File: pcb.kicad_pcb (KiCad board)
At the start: 2 copper layers, 65 x 56 mm, 37 parts, among them J1 Raspberry_Pi_2_3, J10 Conn_01x03_Male, J2 Conn_01x03_Male, J3 Conn_01x03_Male, J4 Conn_01x02_Male, J5 Conn_01x02_Male, J6 Conn_01x03_Male, J7 Conn_01x05_Male, J8 Conn_01x03_Male, J9 Conn_01x03_Male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

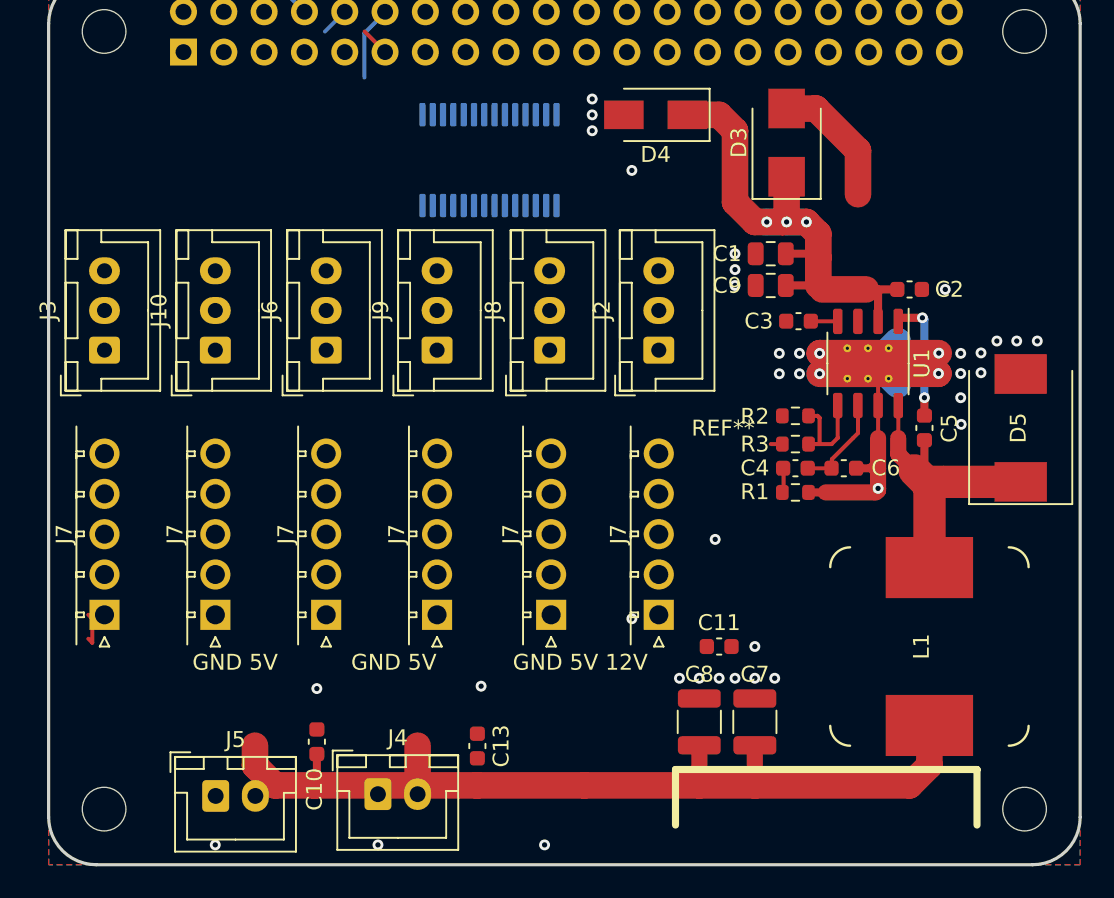
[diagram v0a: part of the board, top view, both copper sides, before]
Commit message: added images & plug placement
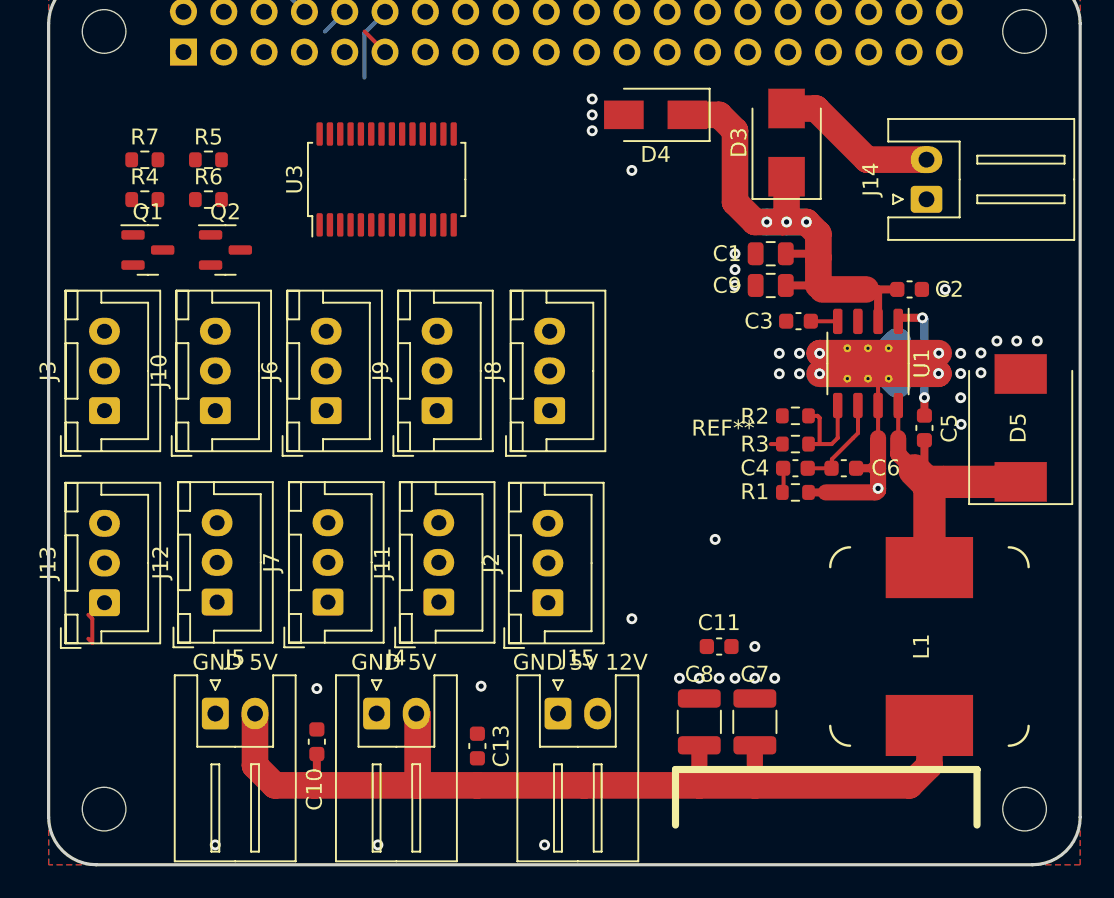
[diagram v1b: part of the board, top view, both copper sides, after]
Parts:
- removed the J7 at (96.5, 111.3)
- removed the J7 at (103.5, 111.3)
- removed the J7 at (110.5, 111.3)
- removed the J7 at (124.7, 111.3)
- removed the J7 at (131.4, 111.3)
- removed the J7 at (117.5, 111.3)
- added J11: Conn_01x03_Male, Connector_JST:JST_XH_B3B-XH-A_1x03_P2.50mm_Vertical, F.Cu at (117.6, 110.5)
- added J12: Conn_01x03_Male, Connector_JST:JST_XH_B3B-XH-A_1x03_P2.50mm_Vertical, F.Cu at (103.6, 110.5)
- added J13: Conn_01x03_Male, Connector_JST:JST_XH_B3B-XH-A_1x03_P2.50mm_Vertical, F.Cu at (96.5, 110.5)
- added J14: Conn_01x02_Male, Connector_JST:JST_XH_S2B-XH-A_1x02_P2.50mm_Horizontal, F.Cu at (148.3, 85.1)
- added J15: Conn_01x02_Male, Connector_JST:JST_XH_S2B-XH-A_1x02_P2.50mm_Horizontal, F.Cu at (125.1, 117.5)
- added J7: Conn_01x03_Male, Connector_JST:JST_XH_B3B-XH-A_1x03_P2.50mm_Vertical, F.Cu at (110.6, 110.5)
- added Q1: Q_NMOS_GSD, Package_TO_SOT_SMD:SOT-23, F.Cu at (99.2, 88.3)
- added Q2: Q_NMOS_GSD, Package_TO_SOT_SMD:SOT-23, F.Cu at (104.1, 88.3)
- added R4: R, Resistor_SMD:R_0603_1608Metric, F.Cu at (99.1, 85.1)
- added R5: R, Resistor_SMD:R_0603_1608Metric, F.Cu at (103.1, 82.6)
- added R6: R, Resistor_SMD:R_0603_1608Metric, F.Cu at (103.1, 85.1)
- added R7: R, Resistor_SMD:R_0603_1608Metric, F.Cu at (99.1, 82.6)
- J4, J5: footprint Connector_JST:JST_XH_B2B-XH-A_1x02_P2.50mm_Vertical -> Connector_JST:JST_XH_S2B-XH-A_1x02_P2.50mm_Horizontal
- U3: moved to F.Cu
- moved J2 17.4 mm to (124.5, 110.5)
- moved U3 6.59 mm to (114.3, 83.8)
- moved J5 5.19 mm to (103.5, 117.5)
- moved J4 5.08 mm to (113.7, 117.5)
- moved J10 3.81 mm to (103.5, 98.4)
- moved J3 3.81 mm to (96.5, 98.4)
- moved J6 3.81 mm to (110.5, 98.4)
- moved J8 3.81 mm to (124.6, 98.4)
- moved J9 3.81 mm to (117.5, 98.4)
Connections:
- J1 pad 3: unconnected-(J1-Pad3) -> LV_SDA
- J1 pad 5: unconnected-(J1-Pad5) -> LV_SCL
- J10 pad 1: unconnected-(J10-Pad1) -> GNDD
- J10 pad 2: unconnected-(J10-Pad2) -> PWM5
- J10 pad 3: unconnected-(J10-Pad3) -> +5V
- J2 pad 1: unconnected-(J2-Pad1) -> GNDD
- J2 pad 2: unconnected-(J2-Pad2) -> PWM1
- J2 pad 3: unconnected-(J2-Pad3) -> +5V
- J3 pad 1: unconnected-(J3-Pad1) -> GNDD
- J3 pad 2: unconnected-(J3-Pad2) -> PWM0
- J3 pad 3: unconnected-(J3-Pad3) -> +5V
- J6 pad 2: unconnected-(J6-Pad2) -> PWM2
- J8 pad 1: unconnected-(J8-Pad1) -> GNDD
- J8 pad 2: unconnected-(J8-Pad2) -> PWM3
- J8 pad 3: unconnected-(J8-Pad3) -> +5V
- J9 pad 1: unconnected-(J9-Pad1) -> GNDD
- J9 pad 2: unconnected-(J9-Pad2) -> PWM4
- J9 pad 3: unconnected-(J9-Pad3) -> +5V
- U3 pad 10: unconnected-(U3-Pad10) -> PWM4
- U3 pad 11: unconnected-(U3-Pad11) -> PWM5
- U3 pad 12: unconnected-(U3-Pad12) -> PWM6
- U3 pad 13: unconnected-(U3-Pad13) -> PWM7
- U3 pad 14: unconnected-(U3-Pad14) -> GNDD
- U3 pad 15: unconnected-(U3-Pad15) -> PWM8
- U3 pad 16: unconnected-(U3-Pad16) -> PWM9
- U3 pad 23: unconnected-(U3-Pad23) -> GNDD
- U3 pad 25: unconnected-(U3-Pad25) -> GNDD
- U3 pad 26: unconnected-(U3-Pad26) -> SCL
- U3 pad 27: unconnected-(U3-Pad27) -> SDA
- U3 pad 28: unconnected-(U3-Pad28) -> +5V
- U3 pad 6: unconnected-(U3-Pad6) -> PWM0
- U3 pad 7: unconnected-(U3-Pad7) -> PWM1
- U3 pad 8: unconnected-(U3-Pad8) -> PWM2
- U3 pad 9: unconnected-(U3-Pad9) -> PWM3
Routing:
- net +5V: track 58.3 -> 62.4 mm, vias 0 -> 1
- net +12V: track 8.35 -> 10.1 mm
- net unconnected-(J7-Pad3): vias 1 -> 0

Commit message: added reverse current protection
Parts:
- added Q3: MMBT3906, Package_TO_SOT_SMD:SOT-23, F.Cu at (122.4, 85.4)
- added Q4: Q_PMOS_GSD, Package_TO_SOT_SMD:SOT-23, F.Cu at (132.1, 86.4)
- added Q5: MMBT3906, Package_TO_SOT_SMD:SOT-23, F.Cu at (127.2, 85.4)
- added R8: 10K, Resistor_SMD:R_0603_1608Metric, F.Cu at (125.9, 88.9)
- added R9: 47K, Resistor_SMD:R_0603_1608Metric, F.Cu at (121.9, 88.9)
- R4, R5, R6, R7: value R -> 10K
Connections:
- J10 pad 3: +5V -> SERVO
- J11 pad 3: +5V -> SERVO
- J12 pad 3: +5V -> SERVO
- J13 pad 3: +5V -> SERVO
- J2 pad 3: +5V -> SERVO
- J3 pad 3: +5V -> SERVO
- J6 pad 3: +5V -> SERVO
- J7 pad 3: +5V -> SERVO
- J8 pad 3: +5V -> SERVO
- J9 pad 3: +5V -> SERVO

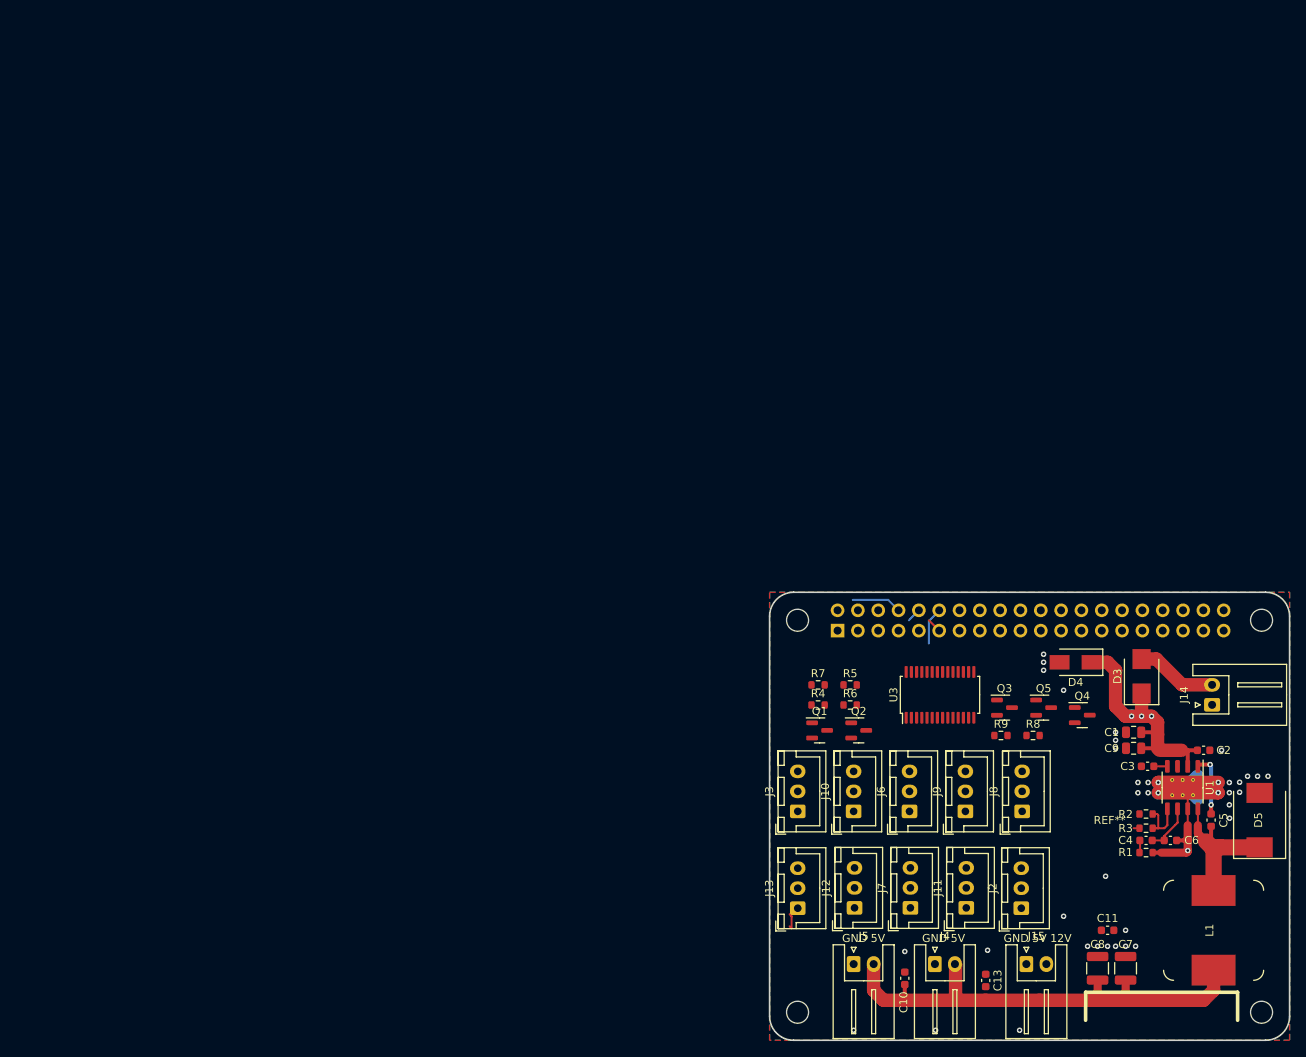
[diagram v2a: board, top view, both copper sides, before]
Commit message: FInalized layout
DRC checked
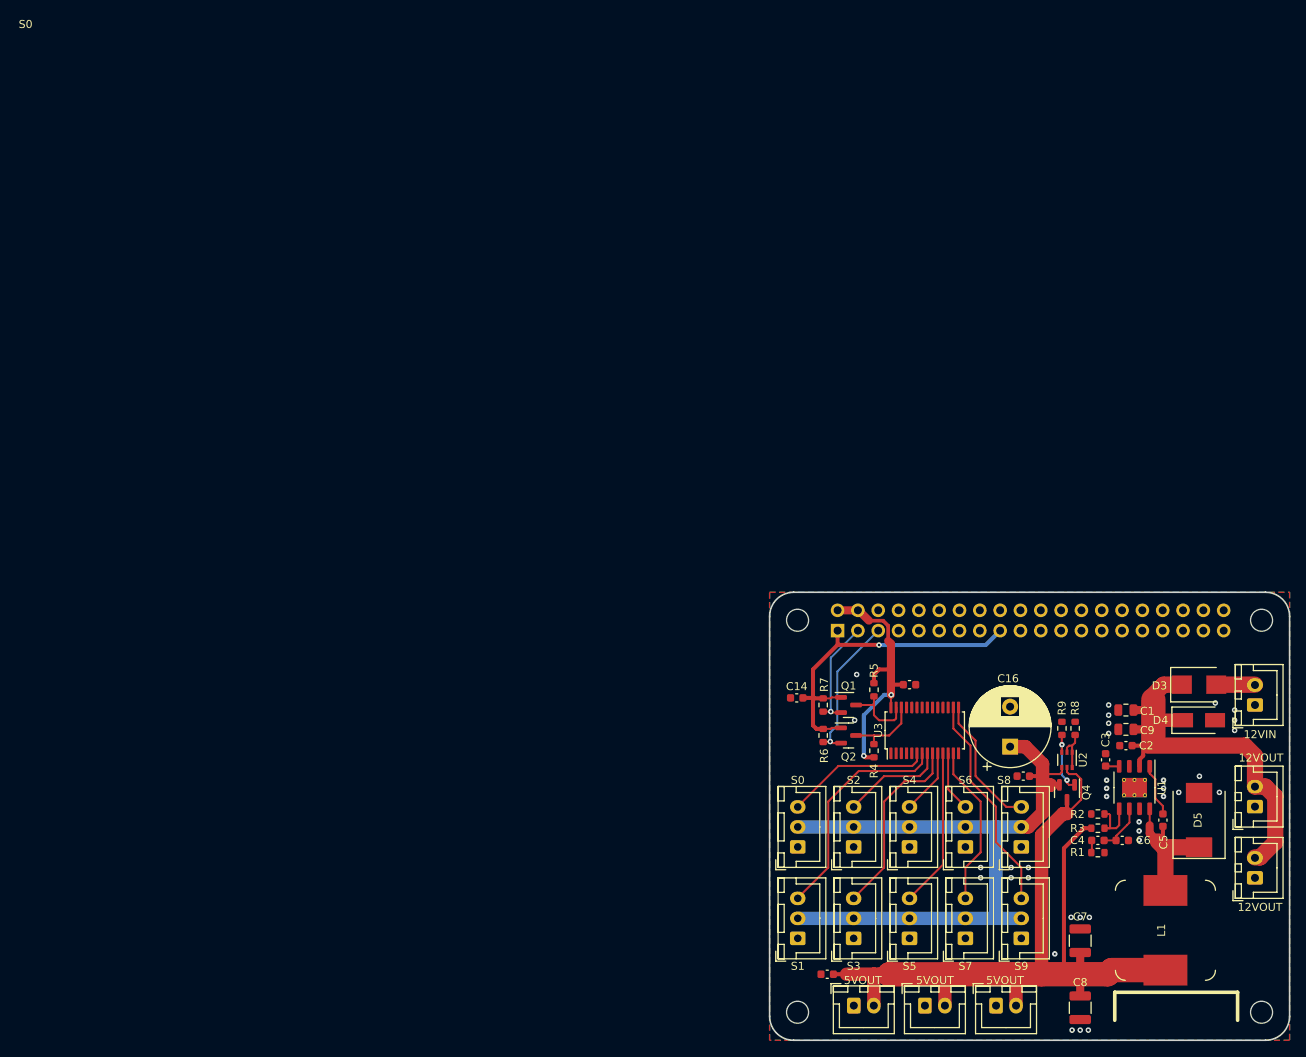
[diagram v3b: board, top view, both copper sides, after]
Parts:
- removed C11, C13: 100n, Capacitor_SMD:C_0603_1608Metric
- removed Q3, Q5: MMBT3906, Package_TO_SOT_SMD:SOT-23
- added C12: 100n, Capacitor_SMD:C_0603_1608Metric, F.Cu at (110.5, 82.5)
- added C14: 100n, Capacitor_SMD:C_0603_1608Metric, F.Cu at (96.4, 84.2)
- added C15: 100n, Capacitor_SMD:C_0603_1608Metric, F.Cu at (124.7, 94.0)
- added C16: 330uF, Capacitor_THT:CP_Radial_D10.0mm_P5.00mm, F.Cu at (123.1, 90.3)
- added J16: Conn_01x02_Male, Connector_JST:JST_XH_B2B-XH-A_1x02_P2.50mm_Vertical, F.Cu at (153.7, 97.8)
- added J17: Conn_01x02_Male, Connector_JST:JST_XH_B2B-XH-A_1x02_P2.50mm_Vertical, F.Cu at (121.3, 122.7)
- added U2: DMMT3906W-7-F, Package_TO_SOT_SMD:SOT-363_SC-70-6, F.Cu at (130.2, 91.9)
- J14, J15, J4, J5: footprint Connector_JST:JST_XH_S2B-XH-A_1x02_P2.50mm_Horizontal -> Connector_JST:JST_XH_B2B-XH-A_1x02_P2.50mm_Vertical
- Q1: value Q_NMOS_GSD -> SI2306
- Q2: value Q_NMOS_GSD -> Si2306
- Q4: value Q_PMOS_GSD -> AO3407
- R9: value 47K -> 47k
- moved J15 30.5 mm to (153.7, 106.7), turned to 90 degrees
- moved J13 28.2 mm to (124.5, 114.3)
- moved J2 28.2 mm to (96.5, 114.3)
- moved J8 26.4 mm to (103.5, 114.3)
- moved J12 22.2 mm to (124.5, 102.8)
- moved J10 17.3 mm to (110.5, 114.3)
- moved D4 17.1 mm to (146.7, 87.0), turned to 0 degrees
- moved J7 10.3 mm to (117.5, 102.8)
- moved Q4 9.84 mm to (130.2, 96.0), turned to -90 degrees
- moved C2 9.73 mm to (137.5, 90.2), turned to 180 degrees
- moved C10 9.71 mm to (100.2, 118.7), turned to 180 degrees
- moved R4 9.03 mm to (106.0, 90.8), turned to -90 degrees
- moved J6 8.28 mm to (103.5, 102.8)
- moved J9 8.28 mm to (110.5, 102.8)
- moved R9 7.67 mm to (129.5, 88.0), turned to -90 degrees
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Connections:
- J1 pad 2: unconnected-(J1-Pad2) -> 5VPi
- J1 pad 4: unconnected-(J1-Pad4) -> 5VPi
- J10 pad 2: PWM5 -> SERVO
- J10 pad 3: SERVO -> PWM5
- J11 pad 2: PWM7 -> SERVO
- J11 pad 3: SERVO -> PWM7
- J12 pad 2: PWM8 -> SERVO
- J12 pad 3: SERVO -> PWM8
- J13 pad 2: PWM9 -> SERVO
- J13 pad 3: SERVO -> PWM9
- J2 pad 2: PWM1 -> SERVO
- J2 pad 3: SERVO -> PWM1
- J3 pad 2: PWM0 -> SERVO
- J3 pad 3: SERVO -> PWM0
- J6 pad 2: PWM2 -> SERVO
- J6 pad 3: SERVO -> PWM2
- J7 pad 2: PWM6 -> SERVO
- J7 pad 3: SERVO -> PWM6
- J8 pad 2: PWM3 -> SERVO
- J8 pad 3: SERVO -> PWM3
- J9 pad 2: PWM4 -> SERVO
- J9 pad 3: SERVO -> PWM4
- Q4 pad 1: Net-(Q4-Pad1) -> Net-(R9-Pad2)
- R4 pad 2: +5V -> 5VPi
- R5 pad 2: +5V -> 5VPi
- R8 pad 1: Net-(Q3-Pad1) -> GNDD
- R8 pad 2: GNDD -> Net-(R8-Pad2)
- R9 pad 1: Net-(Q4-Pad1) -> GNDD
- R9 pad 2: GNDD -> Net-(R9-Pad2)
- U3 pad 1: unconnected-(U3-Pad1) -> GNDD
- U3 pad 2: unconnected-(U3-Pad2) -> GNDD
- U3 pad 24: unconnected-(U3-Pad24) -> GNDD
- U3 pad 28: +5V -> 5VPi
- U3 pad 3: unconnected-(U3-Pad3) -> GNDD
- U3 pad 4: unconnected-(U3-Pad4) -> GNDD
- U3 pad 5: unconnected-(U3-Pad5) -> GNDD
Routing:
- net SERVO: track 0.00 -> 88.4 mm
- net GNDD: track 48.6 -> 0.00 mm, vias 38 -> 35
- net +5V: track 62.4 -> 110.9 mm, vias 1 -> 0
- net +3.3V: track 0.00 -> 42.9 mm, vias 0 -> 1
- net 5VPi: track 0.00 -> 33.0 mm, vias 0 -> 2
- net PWM1: track 0.00 -> 28.6 mm
- net PWM9: track 0.00 -> 27.3 mm
- net PWM3: track 0.00 -> 23.7 mm
- net PWM7: track 0.00 -> 20.3 mm
- net PWM5: track 0.00 -> 19.8 mm
- net +12P: track 34.8 -> 53.6 mm, vias 3 -> 0
- net LV_SCL: track 0.12 -> 18.6 mm, vias 0 -> 1
- net PWM0: track 0.00 -> 18.2 mm
- net PWM8: track 0.00 -> 16.8 mm
- net LV_SDA: track 0.42 -> 13.8 mm, vias 0 -> 1
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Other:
- board text added: "12VIN"
- board text added: "12VOUT"
- board text added: "5VOUT"
- board text added: "S0"
- board text added: "S1"
- board text added: "S2"
- board text added: "S3"
- board text added: "S4"
- board text added: "S5"
- board text added: "S6"
- board text added: "S7"
- board text added: "S8"
- board text added: "S9"
- board text removed: "GND 5V"
- board text removed: "GND 5V 12V"

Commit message: added logos
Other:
- board text added: "HEPHAESTUS ROBOTICS"
- board text added: "TALOS 3"
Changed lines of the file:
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@@
   (net 59 "SERVO")
   (net 60 "+5V")
-  (net 61 "Net-(R9-Pad2)")
+  (net 61 "Net-(Q4-Pad1)")
   (net 62 "Net-(R8-Pad2)")
   (footprint "Diode_SMD:D_SMC" (layer "F.Cu")
@@
       (net 2 "GNDD") (pintype "passive"))
     (pad "2" smd roundrect (at 0.825 0 270) (size 0.8 0.95) (layers "F.Cu" "F.Paste" "F.Mask") (roundrect_rratio 0.25)
-      (net 61 "Net-(R9-Pad2)") (pintype "passive"))
+      (net 61 "Net-(Q4-Pad1)") (pintype "passive"))
     (model "${KICAD6_3DMODEL_DIR}/Resistor_SMD.3dshapes/R_0603_1608Metric.wrl"
       (offset (xyz 0 0 0))
@@
     (fp_line (start -0.65 -1.125) (end -0.325 -1.45) (layer "F.Fab") (width 0.1))
     (pad "1" smd roundrect (at -0.9375 -0.95 270) (size 1.475 0.6) (layers "F.Cu" "F.Paste" "F.Mask") (roundrect_rratio 0.25)
-      (net 61 "Net-(R9-Pad2)") (pinfunction "G") (pintype "input"))
+      (net 61 "Net-(Q4-Pad1)") (pinfunction "G") (pintype "input"))
     (pad "2" smd roundrect (at -0.9375 0.95 270) (size 1.475 0.6) (layers "F.Cu" "F.Paste" "F.Mask") (roundrect_rratio 0.25)
       (net 59 "SERVO") (pinfunction "S") (pintype "passive"))
@@
       (net 62 "Net-(R8-Pad2)") (pinfunction "B1") (pintype "passive"))
     (pad "3" smd rect (at -0.95 0.65 270) (size 0.65 0.4) (layers "F.Cu" "F.Paste" "F.Mask")
-      (net 61 "Net-(R9-Pad2)") (pinfunction "C1") (pintype "passive"))
+      (net 61 "Net-(Q4-Pad1)") (pinfunction "C1") (pintype "passive"))
     (pad "4" smd rect (at 0.95 0.65 270) (size 0.65 0.4) (layers "F.Cu" "F.Paste" "F.Mask")
       (net 59 "SERVO") (pinfunction "E1") (pintype "passive"))
@@
     )
   )
-  (gr_line (start 136.144 121) (end 151.5 121) (layer "F.SilkS") (width 0.45))
-  (gr_line (start 151.5 121) (end 151.5 124.5) (layer "F.SilkS") (width 0.45))
-  (gr_line (start 136.144 124.5) (end 136.144 121) (layer "F.SilkS") (width 0.45))
+  (gr_line (start 136.144 121.031) (end 151.511 121.031) (layer "F.SilkS") (width 0.45))
+  (gr_line (start 151.511 121.031) (end 151.511 126.111) (layer "F.SilkS") (width 0.45))
+  (gr_line (start 136.017 124.079) (end 136.144 124.5) (layer "F.SilkS") (width 0.15))
+  (gr_line (start 136.144 126.111) (end 136.144 121.031) (layer "F.SilkS") (width 0.45))
+  (gr_line (start 151.511 126.111) (end 136.144 126.111) (layer "F.SilkS") (width 0.45))
   (gr_circle (center 133.5 109) (end 133.5 106.5) (layer "Cmts.User") (width 0.15) (fill none))
   (gr_arc (start 126.743262 103.465156) (mid 128.219082 103.227744) (end 129.599999 103.800001) (layer "Cmts.User") (width 0.15))
@@
     (effects (font (size 1 1) (thickness 0.25)))
   )
+  (gr_text "HEPHAESTUS ROBOTICS" (at 125.73 78.867) (layer "F.SilkS")
+    (effects (font (size 1.27 1.27) (thickness 0.15)))
+  )
+  (gr_text "TALOS 3\n" (at 143.764 123.698) (layer "F.SilkS")
+    (effects (font (size 1.7794 1.7794) (thickness 0.3)))
+  )
   (gr_text "S9" (at 124.46 117.729) (layer "F.SilkS")
